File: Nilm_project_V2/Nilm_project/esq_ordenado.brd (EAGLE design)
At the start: 53.4 x 51.7 mm, 37 parts, among them IC1 LM1117IMPX-3.3, Q1 SMD-TRANSISTORS-NPN-25V-500MW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, Q2 SMD-TRANSISTORS-NPN-25V-500MW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, U1 ESP-32S, U2 CP2102-GM, U3 TPD2S017DBVR, U4 SP0503BAHT

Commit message: actualizacion de datahseets, lista de elementos, esquematico terminado
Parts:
- removed X2: (no value), BeagleBone_Blue_R3:GHI-CONNECTORS_10118192-0001LF(MICRO-USB-B-AMPHENOL-FCI)
- added C11: 0.01uF, resistor:C0805
- added C12: 10nF, resistor:C0805
- added R10, R11, R12, R13, R9: 5K, resistor:R0805
- added R14: 1M, resistor:R0805
- added U$1: MICRO_USB_B-AMPHENOL(10118192), usb_microB_10118192:MICRO_B_10118192
- added U5: TMP275AIDR, Sensor:TMP275AIDR
- added U6: INA157U/2K5, INA157U_2K5:SOIC8_INA157U_2K5
- added X3: (no value), con-molex:KK-156-3
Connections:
- new net N$11: R12.2, R13.1, U6.P$2
- new net N$12: R13.2, U6.P$6
- new net N$7: C12.1, R14.2, U$1.SHEL1, U$1.SHEL2, U$1.SHEL3, U$1.SHEL4, U$1.SHEL5, U$1.SHEL6
- new net V+: U6.P$7, X3.1
- new net V-: U6.P$4, X3.3
- net 3.3V: now also C11.1, R10.1, R11.1, R9.1, U5.8
- net CLK: now also R10.2, U5.2
- net D+_OUT: now also U$1.P3; no longer X2.D+
- net D-_OUT: now also U$1.P2; no longer X2.D-
- net GND: now also C11.2, C12.2, R12.1, R14.1, U$1.P4, U$1.P5, U5.4, U5.5, U5.6, U5.7, X3.2; no longer X2.CGND1, X2.CGND2, X2.CGND3, X2.CGND4, X2.CGND5, X2.CGND6, X2.GND
- net IO15: now also R11.2, U5.3
- net IO4: now also U6.P$3
- net SD1: now also R9.2, U5.1
- net VUSB: now also U$1.P1; no longer X2.VBUS
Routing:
- net D+_OUT: track 19.5 -> 15.7 mm
- net D-_OUT: track 19.3 -> 15.4 mm
- net VUSB: track 60.8 -> 57.9 mm

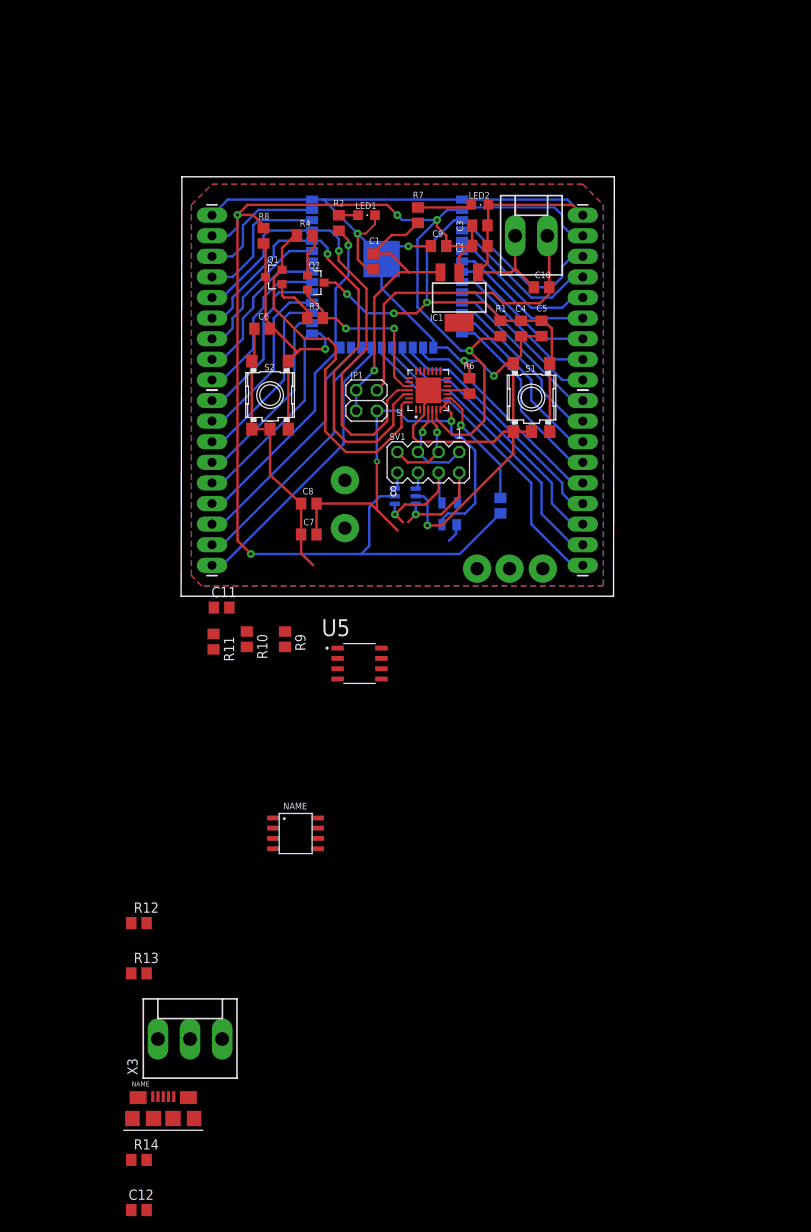
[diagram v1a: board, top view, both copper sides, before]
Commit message: corrección footprint switch tactile y borrado de pistas de la board
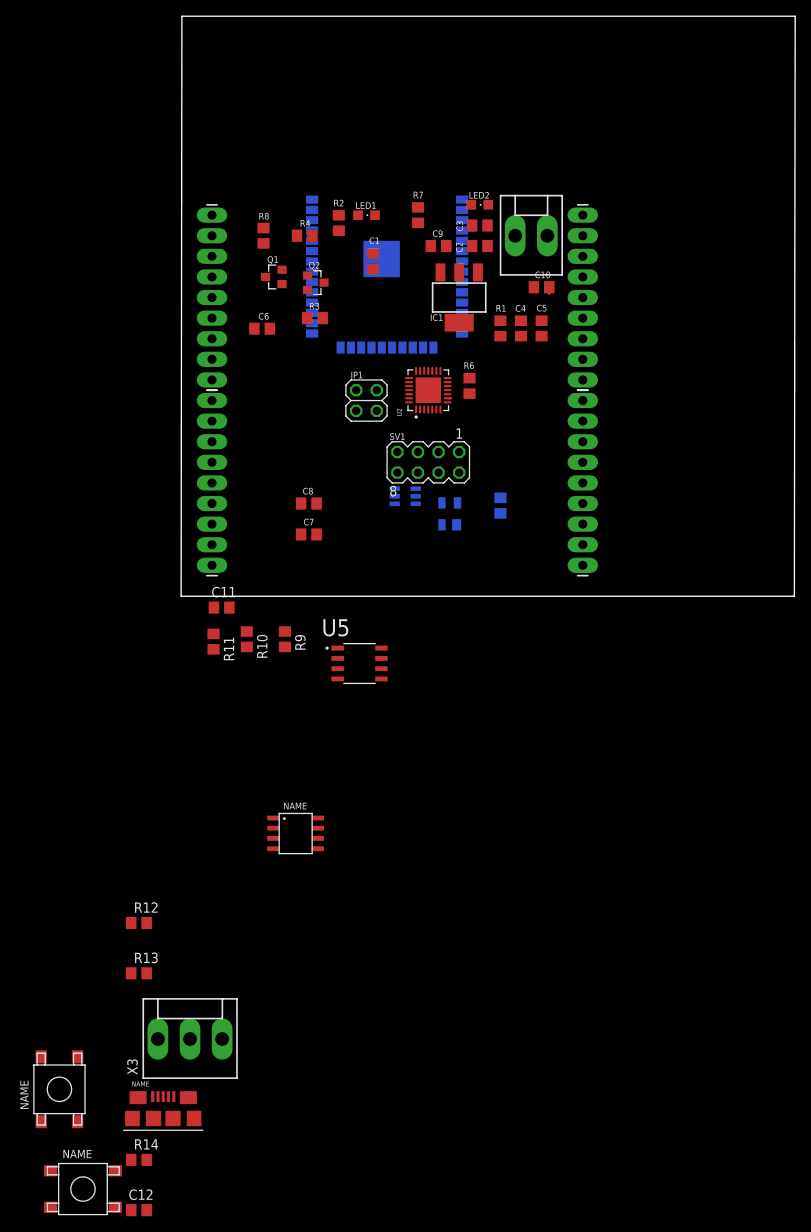
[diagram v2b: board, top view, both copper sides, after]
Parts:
- removed S1, S2: SKHMPSE010, switch:SKHMPXE010
- added S_IO0, U$2: SWITCH_OMRON_B3FS-1012P, switch_B3FS-1012P:B3FS-1012P
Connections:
- net ENABLE: now also U$2.P1, U$2.P2; no longer S1.1, S1.2
- net GND: now also S_IO0.P3, S_IO0.P4, U$2.P3, U$2.P4; no longer S1.3, S1.4, S1.5, S2.3, S2.4, S2.5
- net IO0: now also S_IO0.P1, S_IO0.P2; no longer S2.1, S2.2
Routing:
- net GND: track 235.0 -> 3.61 mm, vias 10 -> 0
- net 3.3V: track 198.0 -> 1.52 mm, vias 5 -> 0
- net TXD_ESP: track 59.2 -> 0.00 mm, vias 1 -> 0
- net RXD_ESP: track 59.1 -> 0.00 mm, vias 1 -> 0
- net VUSB: track 57.9 -> 0.00 mm, vias 2 -> 0
- net IO0: track 58.2 -> 1.14 mm, vias 1 -> 0
- net ENABLE: track 57.1 -> 0.64 mm, vias 3 -> 0
- net DTR_CP: track 46.4 -> 0.32 mm
- net IO2: track 42.3 -> 0.00 mm, vias 1 -> 0
- net VCC: track 40.2 -> 0.82 mm
- net CLK: track 39.3 -> 0.00 mm
- net VIN: track 36.9 -> 0.04 mm, vias 1 -> 0
- net CMD: track 36.3 -> 0.00 mm
- net SD0: track 35.7 -> 0.00 mm
- net SD3: track 33.2 -> 0.00 mm
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- removed copper zone on layer 1, net GND
- removed copper zone on layer 16, net GND
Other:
- board size 53.4 x 51.7 mm -> 75.7 x 71.5 mm
